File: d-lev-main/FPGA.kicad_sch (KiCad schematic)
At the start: 6 parts, among them J2 Tag-Connect TC2030-NL, U1 AC608, U3 25LCxxx

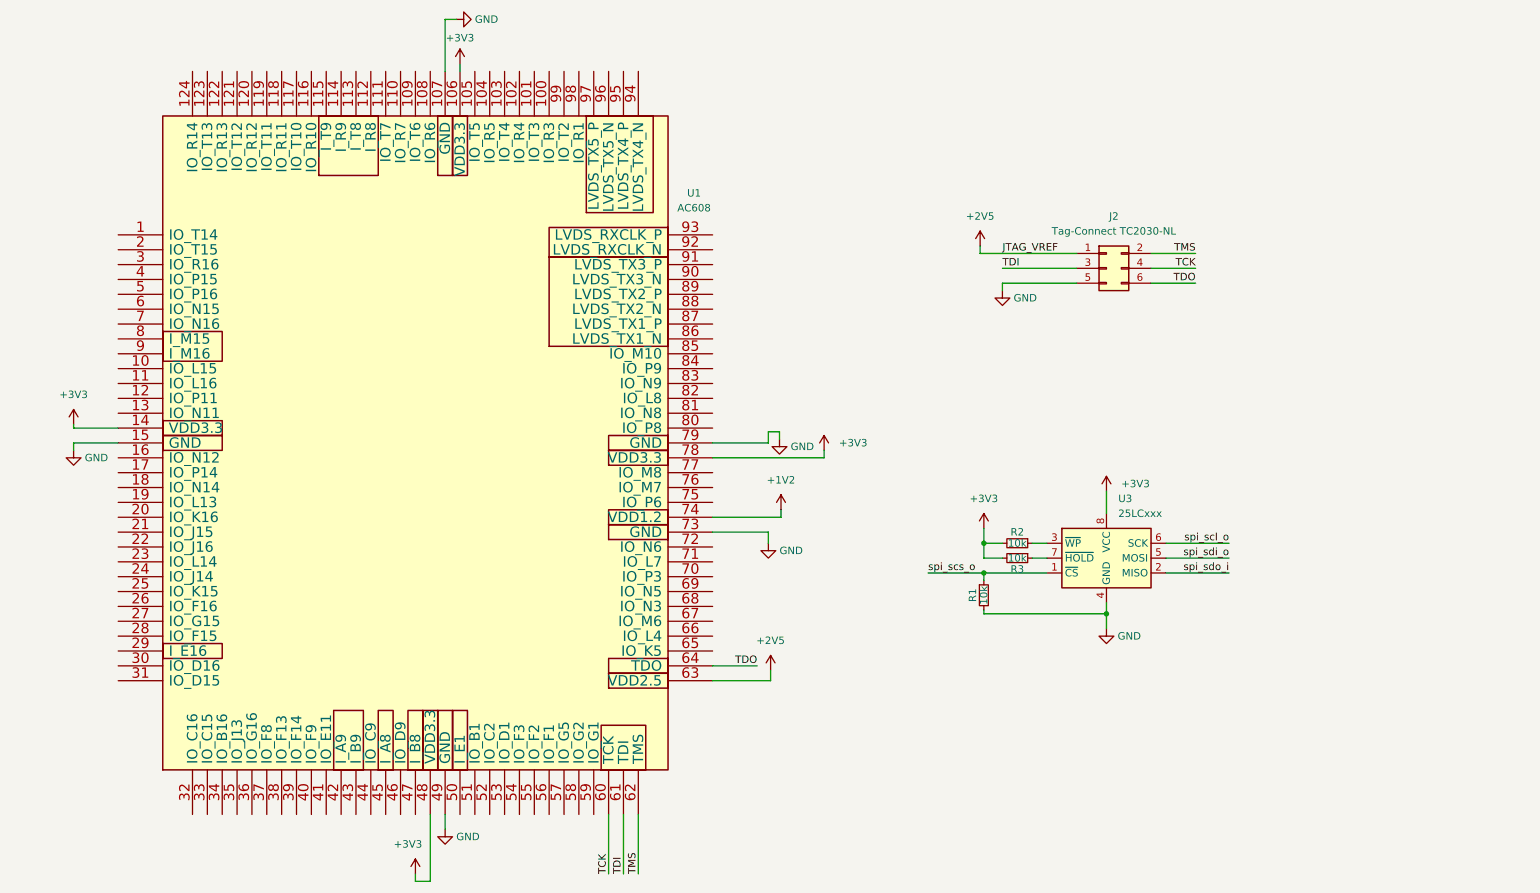
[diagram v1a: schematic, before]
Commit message: Many changes
Reorganized libraries to share between projects
Set up JLC 2- and 4- layer design rules
Finished copying over most of the schematic (excluding I/O board)
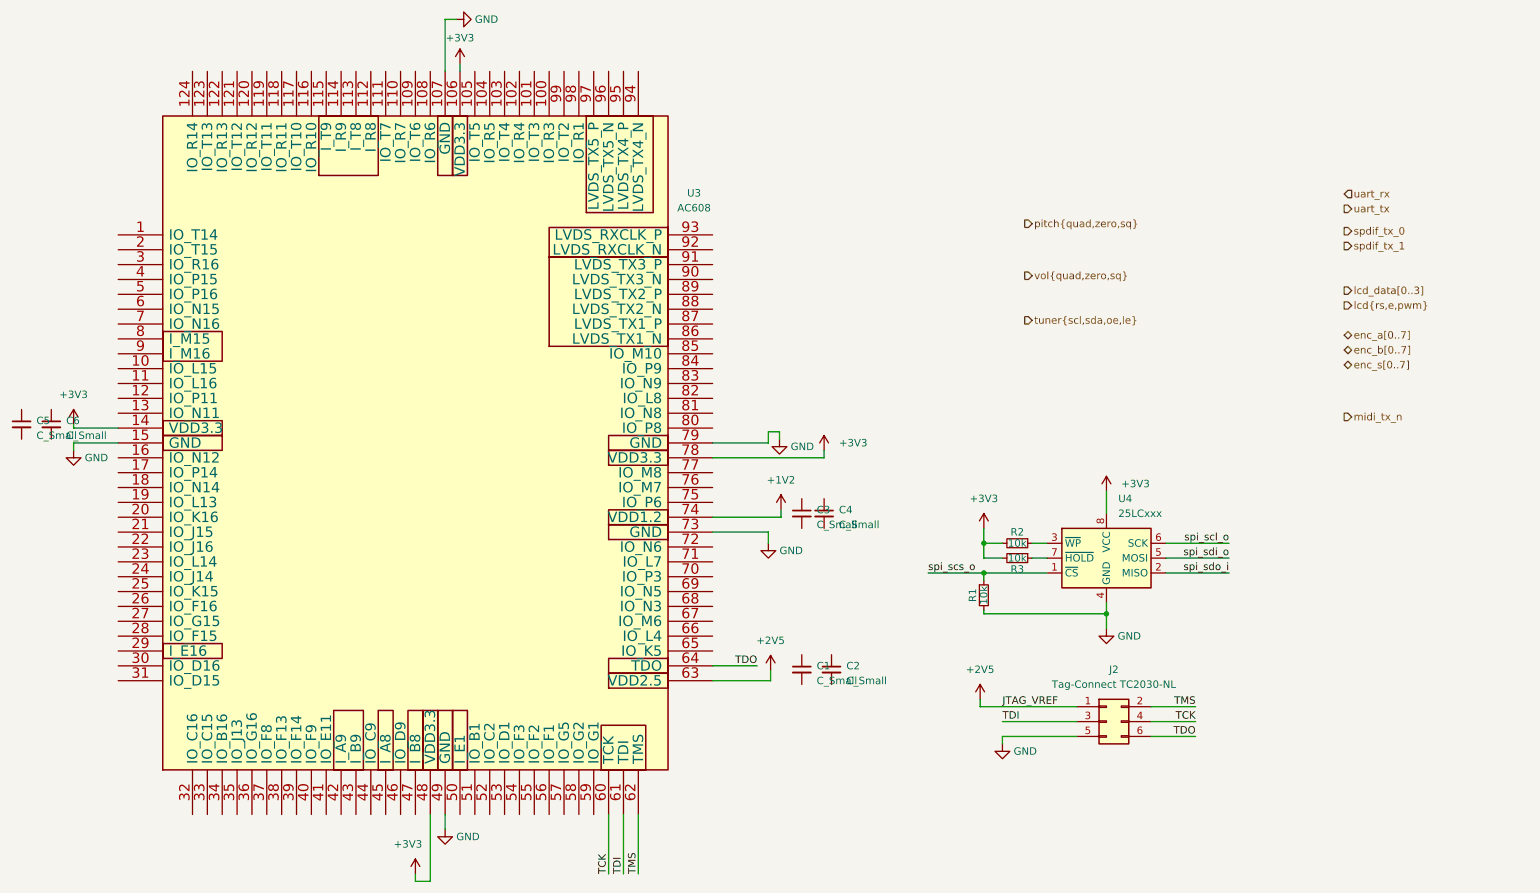
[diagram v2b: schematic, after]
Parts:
- added C1, C2, C3, C4, C5, C6: C_Small, symbol Device:C_Small
- U3: renamed from U1; footprint footprints:ac608 -> d-lev:ac608
- renumbered U3 to U4
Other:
- moved on the sheet: J2

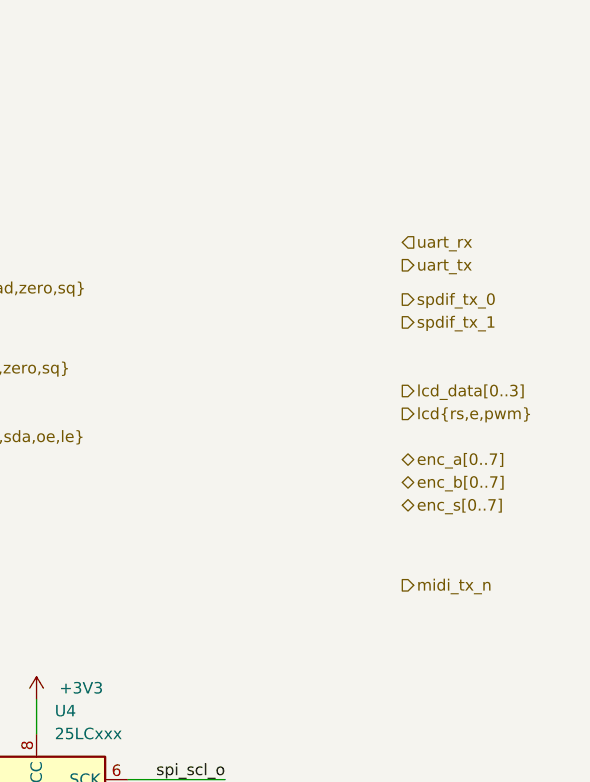
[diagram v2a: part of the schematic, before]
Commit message: schematic + wiring for avr
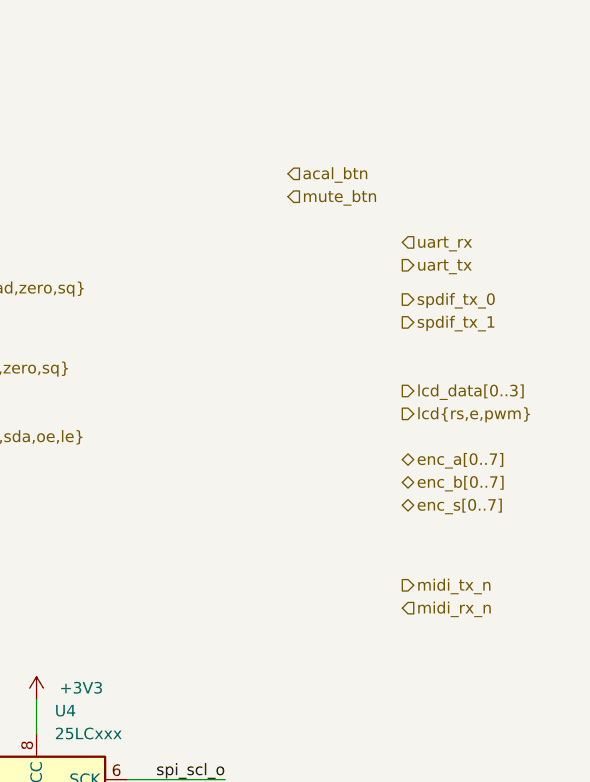
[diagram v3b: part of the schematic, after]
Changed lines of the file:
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@@
+    (effects (font (size 1.27 1.27)) (justify left))
+  )
+  (hierarchical_label "mute_btn" (shape input) (at 238.76 53.34 0) (fields_autoplaced)
     (effects (font (size 1.27 1.27)) (justify left))
   )
@@
     (effects (font (size 1.27 1.27)) (justify left))
   )
+  (hierarchical_label "acal_btn" (shape input) (at 238.76 50.8 0) (fields_autoplaced)
+    (effects (font (size 1.27 1.27)) (justify left))
+  )
   (hierarchical_label "vol{quad,zero,sq}" (shape output) (at 196.85 72.39 0) (fields_autoplaced)
     (effects (font (size 1.27 1.27)) (justify left))
@@
     (effects (font (size 1.27 1.27)) (justify left))
   )
+  (hierarchical_label "midi_rx_n" (shape input) (at 251.46 99.06 0) (fields_autoplaced)
+    (effects (font (size 1.27 1.27)) (justify left))
+  )

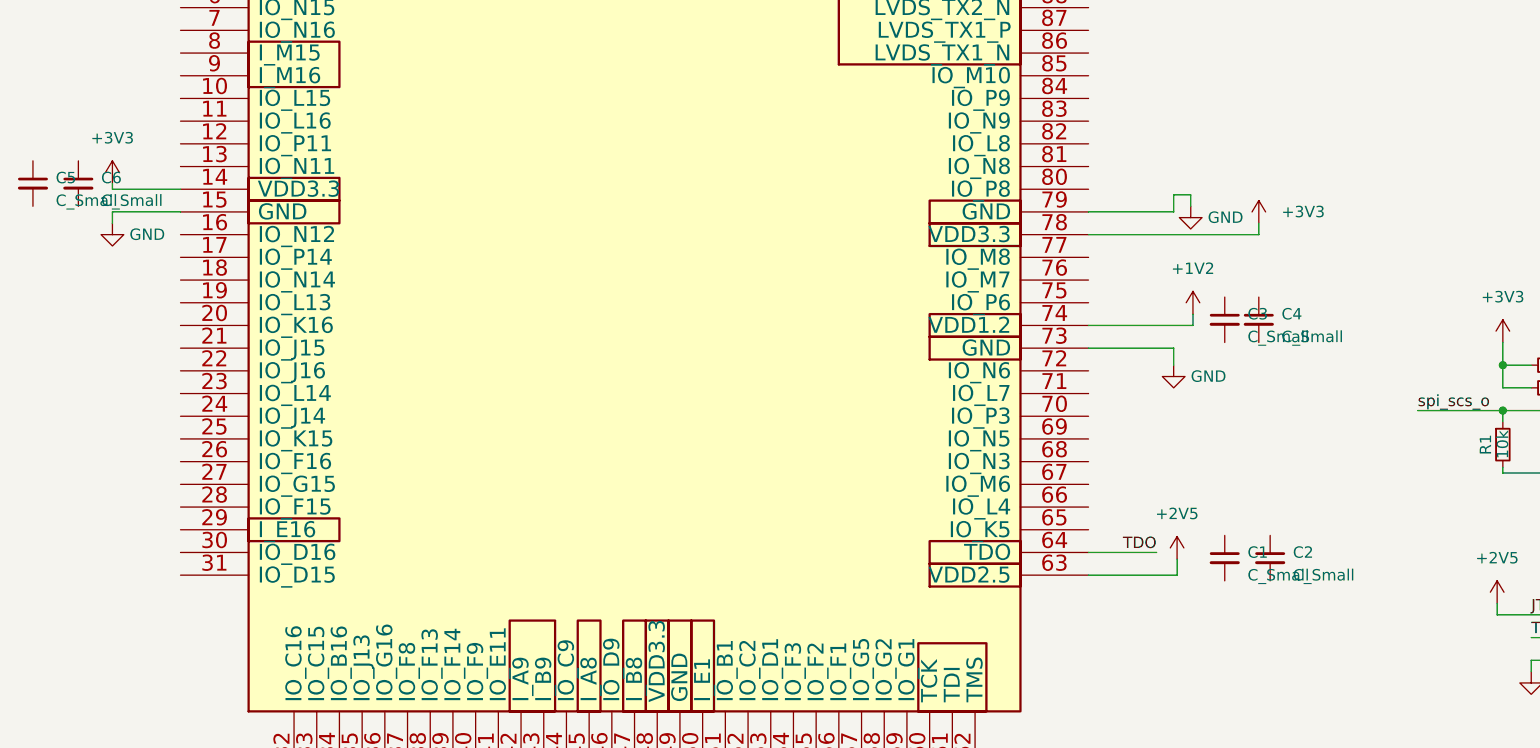
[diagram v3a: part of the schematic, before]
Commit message: clean up 3d models
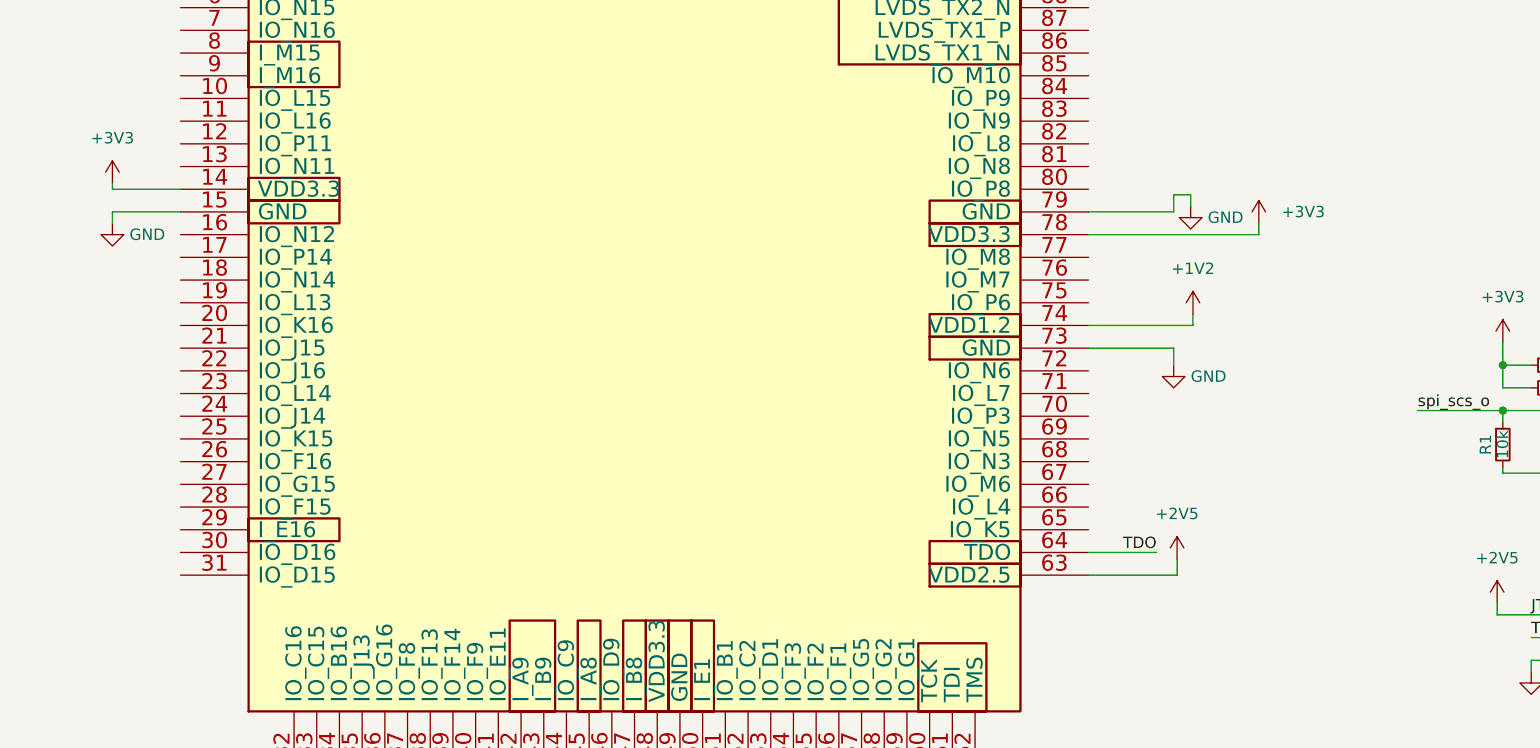
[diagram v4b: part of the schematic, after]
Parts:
- removed C1, C2, C3, C4, C5, C6: C_Small, symbol Device:C_Small
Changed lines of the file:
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@@
 (kicad_sch (version 20230121) (generator eeschema)
   (paper "A4")
+  (bus_alias "tuner" (members "scl" "sda" "oe" "le"))
   (bus_alias "" (members ))
   (bus_alias "" (members ))
-  (bus_alias "tuner" (members "scl" "sda" "oe" "le"))
   (junction (at 210.82 130.175) (diameter 0) (color 0 0 0 0)
   )
@@
     )
   )
-  (symbol (lib_id "Device:C_Small") (at 25.4 97.79 0) (unit 1)
-    (in_bom yes) (on_board yes) (dnp no) (fields_autoplaced)
-    (property "Reference" "C5" (at 27.94 97.1613 0)
-      (effects (font (size 1.27 1.27)) (justify left))
-    )
-    (property "Value" "C_Small" (at 27.94 99.7013 0)
-      (effects (font (size 1.27 1.27)) (justify left))
-    )
-    (property "Footprint" "" (at 25.4 97.79 0)
-      (effects (font (size 1.27 1.27)) hide)
-    )
-    (property "Datasheet" "~" (at 25.4 97.79 0)
-      (effects (font (size 1.27 1.27)) hide)
-    )
-    (pin "1")
-    (pin "2")
-    (instances
-      (project "dlev-mini"
-        (path "/eb5e8bfd-9871-4528-bf57-58851bf63907/acdfb54c-8449-4fbe-9778-47a925c872ef"
-          (reference "C5") (unit 1)
-        )
-      )
-    )
-  )
-  (symbol (lib_id "Device:C_Small") (at 158.75 113.03 0) (unit 1)
-    (in_bom yes) (on_board yes) (dnp no) (fields_autoplaced)
-    (property "Reference" "C3" (at 161.29 112.4013 0)
-      (effects (font (size 1.27 1.27)) (justify left))
-    )
-    (property "Value" "C_Small" (at 161.29 114.9413 0)
-      (effects (font (size 1.27 1.27)) (justify left))
-    )
-    (property "Footprint" "" (at 158.75 113.03 0)
-      (effects (font (size 1.27 1.27)) hide)
-    )
-    (property "Datasheet" "~" (at 158.75 113.03 0)
-      (effects (font (size 1.27 1.27)) hide)
-    )
-    (pin "1")
-    (pin "2")
-    (instances
-      (project "dlev-mini"
-        (path "/eb5e8bfd-9871-4528-bf57-58851bf63907/acdfb54c-8449-4fbe-9778-47a925c872ef"
-          (reference "C3") (unit 1)
-        )
-      )
-    )
-  )
   (symbol (lib_id "power:+2V5") (at 153.416 139.827 0) (unit 1)
     (in_bom yes) (on_board yes) (dnp no) (fields_autoplaced)
@@
         (path "/eb5e8bfd-9871-4528-bf57-58851bf63907/acdfb54c-8449-4fbe-9778-47a925c872ef"
           (reference "#PWR013") (unit 1)
-        )
-      )
-    )
-  )
-  (symbol (lib_id "Device:C_Small") (at 163.83 139.7 0) (unit 1)
-    (in_bom yes) (on_board yes) (dnp no) (fields_autoplaced)
-    (property "Reference" "C2" (at 166.37 139.0713 0)
-      (effects (font (size 1.27 1.27)) (justify left))
-    )
-    (property "Value" "C_Small" (at 166.37 141.6113 0)
-      (effects (font (size 1.27 1.27)) (justify left))
-    )
-    (property "Footprint" "" (at 163.83 139.7 0)
-      (effects (font (size 1.27 1.27)) hide)
-    )
-    (property "Datasheet" "~" (at 163.83 139.7 0)
-      (effects (font (size 1.27 1.27)) hide)
-    )
-    (pin "1")
-    (pin "2")
-    (instances
-      (project "dlev-mini"
-        (path "/eb5e8bfd-9871-4528-bf57-58851bf63907/acdfb54c-8449-4fbe-9778-47a925c872ef"
-          (reference "C2") (unit 1)
         )
       )
@@
         (path "/eb5e8bfd-9871-4528-bf57-58851bf63907/acdfb54c-8449-4fbe-9778-47a925c872ef"
           (reference "#PWR016") (unit 1)
-        )
-      )
-    )
-  )
-  (symbol (lib_id "Device:C_Small") (at 162.56 113.03 0) (unit 1)
-    (in_bom yes) (on_board yes) (dnp no) (fields_autoplaced)
-    (property "Reference" "C4" (at 165.1 112.4013 0)
-      (effects (font (size 1.27 1.27)) (justify left))
-    )
-    (property "Value" "C_Small" (at 165.1 114.9413 0)
-      (effects (font (size 1.27 1.27)) (justify left))
-    )
-    (property "Footprint" "" (at 162.56 113.03 0)
-      (effects (font (size 1.27 1.27)) hide)
-    )
-    (property "Datasheet" "~" (at 162.56 113.03 0)
-      (effects (font (size 1.27 1.27)) hide)
-    )
-    (pin "1")
-    (pin "2")
-    (instances
-      (project "dlev-mini"
-        (path "/eb5e8bfd-9871-4528-bf57-58851bf63907/acdfb54c-8449-4fbe-9778-47a925c872ef"
-          (reference "C4") (unit 1)
         )
       )
@@
     )
   )
-  (symbol (lib_id "Device:C_Small") (at 30.48 97.79 0) (unit 1)
-    (in_bom yes) (on_board yes) (dnp no) (fields_autoplaced)
-    (property "Reference" "C6" (at 33.02 97.1613 0)
-      (effects (font (size 1.27 1.27)) (justify left))
-    )
-    (property "Value" "C_Small" (at 33.02 99.7013 0)
-      (effects (font (size 1.27 1.27)) (justify left))
-    )
-    (property "Footprint" "" (at 30.48 97.79 0)
-      (effects (font (size 1.27 1.27)) hide)
-    )
-    (property "Datasheet" "~" (at 30.48 97.79 0)
-      (effects (font (size 1.27 1.27)) hide)
-    )
-    (pin "1")
-    (pin "2")
-    (instances
-      (project "dlev-mini"
-        (path "/eb5e8bfd-9871-4528-bf57-58851bf63907/acdfb54c-8449-4fbe-9778-47a925c872ef"
-          (reference "C6") (unit 1)
-        )
-      )
-    )
-  )
   (symbol (lib_id "power:+3V3") (at 210.82 109.22 0) (unit 1)
     (in_bom yes) (on_board yes) (dnp no) (fields_autoplaced)
@@
         )
       )
-    )
-  )
-  (symbol (lib_id "Device:C_Small") (at 158.75 139.7 0) (unit 1)
-    (in_bom yes) (on_board yes) (dnp no) (fields_autoplaced)
-    (property "Reference" "C1" (at 161.29 139.0713 0)
-      (effects (font (size 1.27 1.27)) (justify left))
-    )
-    (property "Value" "C_Small" (at 161.29 141.6113 0)
-      (effects (font (size 1.27 1.27)) (justify left))
-    )
-    (property "Footprint" "" (at 158.75 139.7 0)
-      (effects (font (size 1.27 1.27)) hide)
-    )
-    (property "Datasheet" "~" (at 158.75 139.7 0)
-      (effects (font (size 1.27 1.27)) hide)
-    )
-    (pin "1")
-    (pin "2")
-    (instances
-      (project "dlev-mini"
-        (path "/eb5e8bfd-9871-4528-bf57-58851bf63907/acdfb54c-8449-4fbe-9778-47a925c872ef"
-          (reference "C1") (unit 1)
-        )
-      )
